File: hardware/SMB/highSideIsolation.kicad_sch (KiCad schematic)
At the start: 10 parts

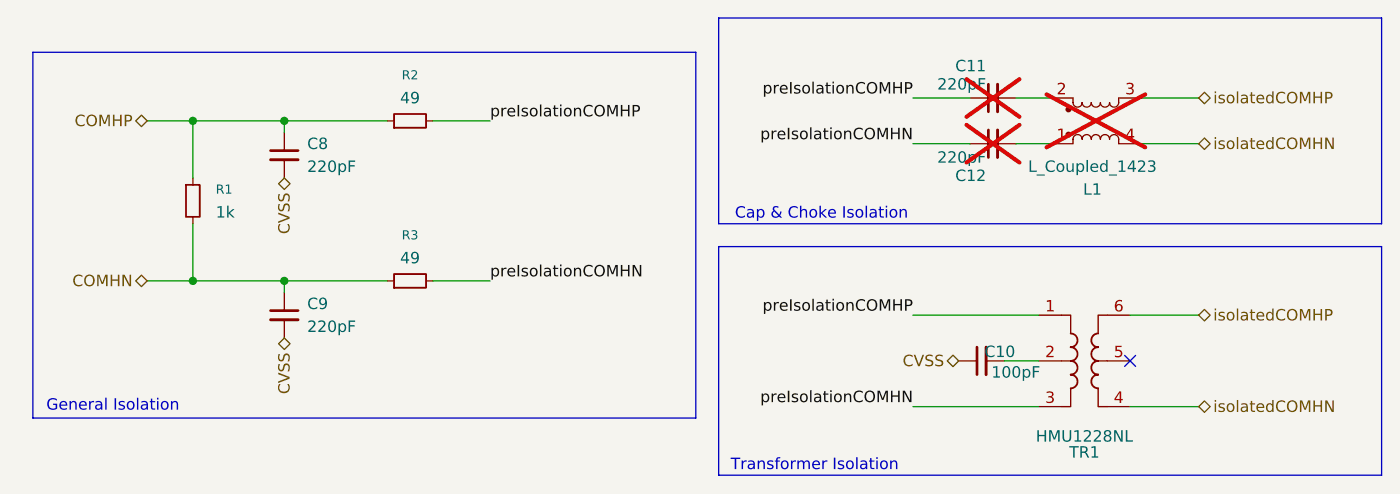
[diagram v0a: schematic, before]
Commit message: added BOM
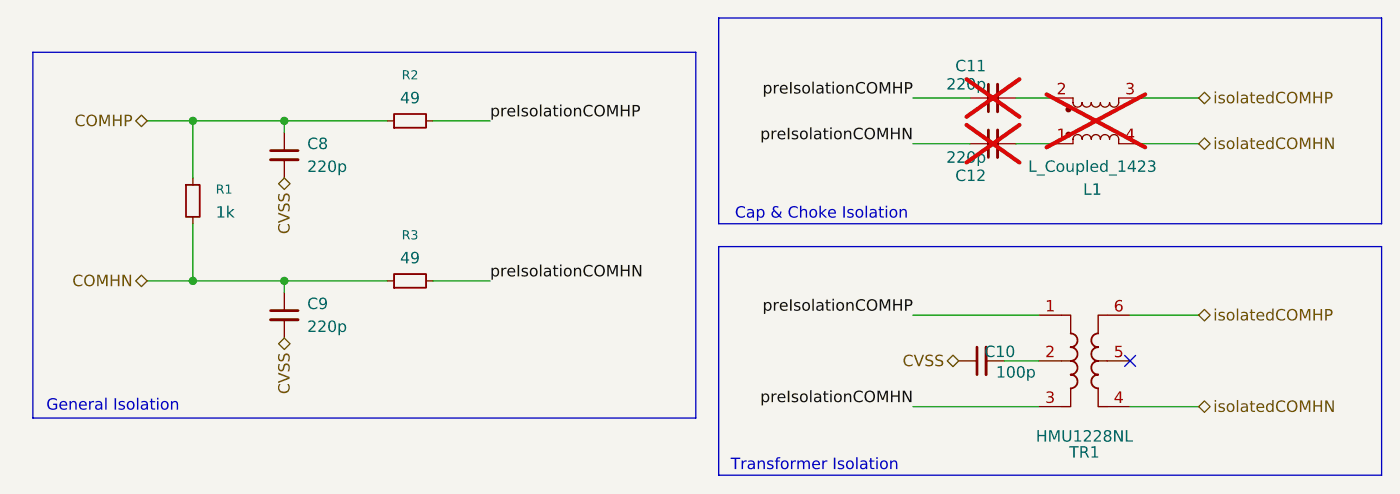
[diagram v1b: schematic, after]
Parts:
- C10: value 100pF -> 100p; P/N (none) -> KGM15AR71C101KT
- C11, C12, C8, C9: value 220pF -> 220p; P/N (none) -> CC0603JRNPO9BN221
- L1: P/N (none) -> 744242471
- R1: P/N (none) -> 0603WAF1001T5E
- R2, R3: P/N (none) -> RC0603FR-0749R9L
- TR1: P/N (none) -> HMU1228NL
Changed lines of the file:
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@@
+			)
+		)
+		(property "P/N" "744242471"
+			(at 186.69 93.98 0)
+			(hide yes)
+			(show_name no)
+			(do_not_autoplace no)
+			(effects
+				(font
+					(size 1.27 1.27)
+				)
 			)
 		)
@@
 			)
 		)
+		(property "P/N" "HMU1228NL"
+			(at 185.42 120.65 0)
+			(hide yes)
+			(show_name no)
+			(do_not_autoplace no)
+			(effects
+				(font
+					(size 1.27 1.27)
+				)
+			)
+		)
 		(pin "4"
 		)
@@
 			)
 		)
-		(property "Value" "220pF"
+		(property "Value" "220p"
 			(at 174.498 89.916 90)
 			(show_name no)
@@
 		(property "Description" "Unpolarized capacitor, small symbol"
 			(at 175.26 91.44 0)
+			(hide yes)
+			(show_name no)
+			(do_not_autoplace no)
+			(effects
+				(font
+					(size 1.27 1.27)
+				)
+			)
+		)
+		(property "P/N" "CC0603JRNPO9BN221"
+			(at 175.26 91.44 90)
 			(hide yes)
 			(show_name no)
@@
 			)
 		)
-		(property "Value" "220pF"
+		(property "Value" "220p"
 			(at 99.06 116.8462 0)
 			(show_name no)
@@
 		)
 		(property "Description" "Unpolarized capacitor, small symbol"
+			(at 96.52 115.57 0)
+			(hide yes)
+			(show_name no)
+			(do_not_autoplace no)
+			(effects
+				(font
+					(size 1.27 1.27)
+				)
+			)
+		)
+		(property "P/N" "CC0603JRNPO9BN221"
 			(at 96.52 115.57 0)
 			(hide yes)
@@
 			)
 		)
-		(property "Value" "220pF"
+		(property "Value" "220p"
 			(at 99.06 99.0662 0)
 			(show_name no)
@@
 		)
 		(property "Description" "Unpolarized capacitor, small symbol"
+			(at 96.52 97.79 0)
+			(hide yes)
+			(show_name no)
+			(do_not_autoplace no)
+			(effects
+				(font
+					(size 1.27 1.27)
+				)
+			)
+		)
+		(property "P/N" "CC0603JRNPO9BN221"
 			(at 96.52 97.79 0)
 			(hide yes)
@@
 			)
 		)
+		(property "P/N" "RC0603FR-0749R9L"
+			(at 110.49 93.98 90)
+			(hide yes)
+			(show_name no)
+			(do_not_autoplace no)
+			(effects
+				(font
+					(size 1.27 1.27)
+				)
+			)
+		)
 		(pin "1"
 		)
@@
 			)
 		)
-		(property "Value" "220pF"
+		(property "Value" "220p"
 			(at 174.498 98.044 90)
 			(show_name no)
@@
 		(property "Description" "Unpolarized capacitor, small symbol"
 			(at 175.26 96.52 0)
+			(hide yes)
+			(show_name no)
+			(do_not_autoplace no)
+			(effects
+				(font
+					(size 1.27 1.27)
+				)
+			)
+		)
+		(property "P/N" "CC0603JRNPO9BN221"
+			(at 175.26 96.52 90)
 			(hide yes)
 			(show_name no)
@@
 			)
 		)
+		(property "P/N" "0603WAF1001T5E"
+			(at 86.36 102.87 0)
+			(hide yes)
+			(show_name no)
+			(do_not_autoplace no)
+			(effects
+				(font
+					(size 1.27 1.27)
+				)
+			)
+		)
 		(pin "1"
 		)
@@
 			)
 		)
-		(property "Value" "100pF"
+		(property "Value" "100p"
 			(at 177.8 121.92 90)
 			(show_name no)
@@
 		(property "Description" "Unpolarized capacitor, small symbol"
 			(at 173.99 120.65 0)
+			(hide yes)
+			(show_name no)
+			(do_not_autoplace no)
+			(effects
+				(font
+					(size 1.27 1.27)
+				)
+			)
+		)
+		(property "P/N" "KGM15AR71C101KT"
+			(at 173.99 120.65 90)
 			(hide yes)
 			(show_name no)
@@
 			(hide yes)
 			(show_name no)
+			(do_not_autoplace no)
+			(effects
+				(font
+					(size 1.27 1.27)
+				)
+			)
+		)
+		(property "P/N" "RC0603FR-0749R9L"
+			(at 110.49 111.76 90)
+			(hide yes)
+			(show_name no)
